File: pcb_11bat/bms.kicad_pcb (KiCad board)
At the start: 2 copper layers, 187 parts, among them CON1 USB-MINI-B, IC1 ATMEGA168PA-M, K1 CONN_3, K2 CONN_3, P1 CONN_1, P10 CONN_1, P11 CONN_1, P12 CONN_1, P13 CONN_1, P14 CONN_1, P15 CONN_1, P16 CONN_1, P17 CONN_1, P18 CONN_1, P19 CONN_1, P2 CONN_1, P20 CONN_1, P21 CONN_2, P22 CONN_1, P23 CONN_1, P3 CONN_1, P4 CONN_1, P5 CONN_1, P6 CONN_1, P7 CONN_3X2, P8 CONN_1, P9 CONN_1, Q1 BC550, Q10 NTD5867, Q11 NTD5867, Q12 NTD5867, Q13 NTD5867, Q14 BC550, Q2 NTD5867, Q3 NTD5867, Q4 NTD5867, Q5 NTD5867, Q6 NTD5867, Q7 NTD5867, Q8 NTD5867, Q9 NTD5867, SW1 SW_PUSH, U1 OPTO, U2 OPTO, U3 AD7280A, U4 AD7280A, U5 LT3010-5, U6 LTC2630, U7 INA197, U8 HRS1K, U9 FT232RQ, X1 CRYSTAL, X2 CRYSTAL 12Mhz

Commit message: placement before routing & corrected a missing resitor on vlow
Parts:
- added R65: 10K, SM0805, F.Cu at (166.5, 68.0)
- added R66: 10K, SM0805, F.Cu at (109.5, 79.0)
- C49: footprint SM0805 -> SMDHD/VF
- moved P2 291.8 mm to (336.5, 88.5)
- moved P3 287.8 mm to (331.0, 88.5)
- moved P21 247.9 mm to (328.0, 51.0)
- moved U2 240.5 mm to (295.0, 51.0), turned to 180 degrees
- moved R42 238.7 mm to (56.5, 81.0)
- moved Q10 236.9 mm to (72.0, 63.0)
- moved U6 233.9 mm to (327.5, 59.0)
- moved U1 231.3 mm to (285.0, 42.0)
- moved P15 229.2 mm to (52.0, 88.0)
- moved K1 226.7 mm to (269.5, 46.0)
- moved P16 219.6 mm to (62.0, 88.0)
- moved P17 209.8 mm to (72.0, 88.5)
- moved SW1 201.8 mm to (277.5, 142.0), turned to 270 degrees
- moved P18 200.4 mm to (82.0, 88.0)
- moved R43 198.7 mm to (66.5, 81.0)
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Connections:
- C21 pad 2: /AD7280A/AD7280A_SUB_LOW/LOBAT -> /AD7280A/AD7280A_SUB_LOW/VIN0
- C35 pad 2: /AD7280A/AD7280A_SUB_LOW/HIBAT -> /AD7280A/AD7280A_SUB_HI/VIN0
- U3 pad 13: /AD7280A/AD7280A_SUB_LOW/LOBAT -> /AD7280A/AD7280A_SUB_LOW/VIN0
- U4 pad 13: /AD7280A/AD7280A_SUB_LOW/HIBAT -> /AD7280A/AD7280A_SUB_HI/VIN0
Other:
- copper layers 2 -> 4
- net class power added: clearance 0.5, trace_width 1, via_dia 0.889, via_drill 0.635
- net class shunts added: clearance 1, trace_width 1.5, via_dia 0.889, via_drill 0.635

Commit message: fixed misplaced caps on the vins, changed some pins assignations on the avr and routed
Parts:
- added R67: 0R, SM0805, F.Cu at (60.5, 135.0)
- added R68: 0R, SM0805, F.Cu at (114.4, 134.6)
- added R69: 0R, SM0805, F.Cu at (52.5, 135.0)
- K1: value CONN_3 -> CHARGER GND 12V SHUT
- K2: value CONN_3 -> REL NC VBAT
- P10: value CONN_1 -> BAT5+
- P11: value CONN_1 -> BAT4+
- P12: value CONN_1 -> BAT3+
- P13: value CONN_1 -> BAT2+
- P14: value CONN_1 -> BAT1+
- P15: value CONN_1 -> VBAT+
- P16: value CONN_1 -> BAT11+/SHUNT
- P17: value CONN_1 -> BAT10+
- P18: value CONN_1 -> BAT9+
- P19: value CONN_1 -> BAT8+
- P20: value CONN_1 -> BAT7+
- P21: value CONN_2 -> GAUGE
- P22: value CONN_1 -> SHUNT
- P23: value CONN_1 -> BAT+
- P8: value CONN_1 -> VBAT GND
- P9: value CONN_1 -> BAT6+
- SP1: value SPEAKER -> BUZZER
- moved D5 159.1 mm to (140.6, 90.6)
- moved C46 152.0 mm to (144.4, 90.4)
- moved R5 145.5 mm to (188.0, 136.7), turned to 180 degrees
- moved U5 145.3 mm to (146.2, 92.0)
- moved C45 138.9 mm to (151.8, 89.5), turned to 270 degrees
- moved P2 138.2 mm to (211.5, 147.5)
- moved R6 135.7 mm to (187.2, 131.1), turned to 270 degrees
- moved C44 135.0 mm to (153.8, 89.5), turned to 270 degrees
- moved U1 133.3 mm to (195.7, 140.9), turned to 180 degrees
- moved C47 133.0 mm to (205.1, 99.3), turned to 180 degrees
- moved U2 132.4 mm to (190.2, 131.9), turned to 0 degrees
- moved R1 126.7 mm to (195.7, 136.4), turned to 90 degrees
- moved U6 126.4 mm to (205.7, 92.8), turned to 180 degrees
- moved P21 125.2 mm to (211.2, 96.0), turned to 270 degrees
- moved C4 121.8 mm to (202.2, 138.9), turned to 270 degrees
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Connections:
- C16 pad 2: N-00000108 (its old number) -> N-00000131
- C17 pad 1: /AD7280A/AD7280A_SUB_LOW/VIN5 -> N-00000131
- C17 pad 2: N-0000097 (its old number) -> /AD7280A/AD7280A_SUB_LOW/VIN4
- C18 pad 2: N-0000094 (its old number) -> /AD7280A/AD7280A_SUB_LOW/VIN3
- C19 pad 2: N-00000103 -> /AD7280A/AD7280A_SUB_LOW/VIN2
- C20 pad 2: N-00000122 (its old number) -> /AD7280A/AD7280A_SUB_LOW/VIN1
- C30 pad 2: N-00000169 -> N-00000168
- C31 pad 1: /AD7280A/AD7280A_SUB_HI/VIN5 -> N-00000168
- C31 pad 2: N-00000170 -> /AD7280A/AD7280A_SUB_HI/VIN4
- C32 pad 2: N-00000173 -> /AD7280A/AD7280A_SUB_HI/VIN3
- C33 pad 2: N-00000171 (its old number) -> /AD7280A/AD7280A_SUB_HI/VIN2
- C34 pad 2: N-00000167 (its old number) -> /AD7280A/AD7280A_SUB_HI/VIN1
- CON1 pad 4: N-0000081 -> (no net)
- CON1 pad 6: /usbserial/SHELL -> /AD7280A/GND
- CON1 pad 7: /usbserial/SHELL -> /AD7280A/GND
- CON1 pad 8: /usbserial/SHELL -> /AD7280A/GND
- CON1 pad 9: /usbserial/SHELL -> /AD7280A/GND
- IC1 pad 1: /CHARGER_ON/ -> /AD7280A/CS/
- IC1 pad 10: /LEDBALANCING -> /LEDERROR
- IC1 pad 11: /LEDERROR -> /BUZZER
- IC1 pad 12: /AD7280A/CS/ -> /STOP_CHARGER
- IC1 pad 13: /BUZZER -> /CHARGER_ON/
- IC1 pad 14: /AD7280A/PD/ -> /comandsolenoid/COILON
- IC1 pad 2: /gauge/CSDAC/ -> /AD7280A/PD/
- IC1 pad 23: /AD7280A/CNVST/ -> (no net)
- IC1 pad 24: (no net) -> /gauge/CSDAC/
- IC1 pad 25: (no net) -> /usbserial/REQUESTTOSEND
- IC1 pad 26: /usbserial/REQUESTTOSEND -> /usbserial/CLEARTOSEND
- IC1 pad 27: /usbserial/CLEARTOSEND -> (no net)
- IC1 pad 28: /comandsolenoid/COILON -> /AD7280A/CNVST/
- IC1 pad 9: /STOP_CHARGER -> /LEDBALANCING
- P10 pad 1: N-00000108 (its old number) -> N-00000106
- P11 pad 1: N-0000097 (its old number) -> N-0000096
- P12 pad 1: N-0000094 (its old number) -> N-00000103
- P13 pad 1: N-00000103 -> N-00000101
- P14 pad 1: N-00000122 (its old number) -> N-00000125
- P18 pad 1: N-00000173 -> N-00000172
- P19 pad 1: N-00000171 (its old number) -> N-00000173
- P20 pad 1: N-00000167 (its old number) -> N-00000166
- Q10 pad 3: N-00000173 -> N-00000172
- Q11 pad 3: N-00000171 (its old number) -> N-00000173
- Q12 pad 3: N-00000167 (its old number) -> N-00000166
- Q2 pad 3: N-00000108 (its old number) -> N-00000106
- Q3 pad 3: N-0000097 (its old number) -> N-0000096
- Q4 pad 3: N-0000094 (its old number) -> N-00000103
- Q5 pad 3: N-00000103 -> N-00000101
- Q6 pad 3: N-00000122 (its old number) -> N-00000125
- R24 pad 1: N-00000108 (its old number) -> N-00000106
- R25 pad 1: N-0000097 (its old number) -> N-0000096
- R26 pad 1: N-0000094 (its old number) -> N-00000103
- R27 pad 1: N-00000103 -> N-00000101
- R28 pad 1: N-00000122 (its old number) -> N-00000125
- R30 pad 1: N-00000108 (its old number) -> N-00000106
- R30 pad 2: /AD7280A/AD7280A_SUB_LOW/VIN5 -> N-00000131
- R31 pad 1: N-0000097 (its old number) -> N-0000096
- R32 pad 1: N-0000094 (its old number) -> N-00000103
- R33 pad 1: N-00000103 -> N-00000101
- R34 pad 1: N-00000122 (its old number) -> N-00000125
- R45 pad 1: N-00000173 -> N-00000172
- R46 pad 1: N-00000171 (its old number) -> N-00000173
- R47 pad 1: N-00000167 (its old number) -> N-00000166
- R49 pad 2: /AD7280A/AD7280A_SUB_HI/VIN5 -> N-00000168
- R51 pad 1: N-00000173 -> N-00000172
- R52 pad 1: N-00000171 (its old number) -> N-00000173
- R53 pad 1: N-00000167 (its old number) -> N-00000166
- R61 pad 1: N-0000081 -> /AD7280A/AD7280A_SUB_LOW/VIN4
- R61 pad 2: /AD7280A/GND -> /AD7280A/AD7280A_SUB_LOW/VIN5
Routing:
- net /AD7280A/GND: track 0.00 -> 424.1 mm, vias 0 -> 13
- net /SHIELD: track 0.00 -> 322.0 mm
- net /CSense/5V: track 0.00 -> 233.4 mm, vias 0 -> 8
- net /AD7280A/AD7280A_SUB_LOW/VDDNFILTERED: track 0.00 -> 230.7 mm, vias 0 -> 4
- net /AD7280A/VBAT: track 0.00 -> 186.5 mm, vias 0 -> 4
- net /AD7280A/AD7280A_SUB_LOW/HIBAT: track 0.00 -> 126.8 mm, vias 0 -> 1
- net /AD7280A/SCLK: track 0.00 -> 126.7 mm, vias 0 -> 4
- net /AD7280A/SDI: track 0.00 -> 123.4 mm, vias 0 -> 4
- net /AD7280A/AD7280A_SUB_LOW/VIN2: track 0.00 -> 100.2 mm, vias 0 -> 3
- net /AD7280A/AD7280A_SUB_LOW/VIN1: track 0.00 -> 93.0 mm, vias 0 -> 3
- net /AD7280A/AD7280A_SUB_LOW/LOBAT: track 0.00 -> 89.9 mm, vias 0 -> 2
- net /AD7280A/SDO: track 0.00 -> 83.3 mm, vias 0 -> 2
- net /AD7280A/AD7280A_SUB_LOW/VIN3: track 0.00 -> 83.0 mm, vias 0 -> 3
- net /AD7280A/AD7280A_SUB_LOW/VIN0: track 0.00 -> 77.8 mm, vias 0 -> 2
- net /AD7280A/AD7280A_SUB_HI/VIN6: track 0.00 -> 75.2 mm, vias 0 -> 2
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- added copper zone on B.Cu, net /AD7280A/AD7280A_SUB_LOW/VDDNFILTERED
- added copper zone on F.Cu, net /AD7280A/AD7280A_SUB_LOW/VDDNFILTERED
- added copper zone on B.Cu, net /AD7280A/GND
- added copper zone on F.Cu, net /AD7280A/GND
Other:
- board outline added: 179.5 x 67 mm
- copper layers 4 -> 2
- net class Default: clearance 0.254 -> 0.1
- net class Oldefault added: clearance 0.254, trace_width 0.254, via_dia 0.889, via_drill 0.635
- net class halfpower added: clearance 0.254, trace_width 0.354, via_dia 0.889, via_drill 0.635
- net class micro added: clearance 0.125, trace_width 0.254, via_dia 0.889, via_drill 0.635
- rule trace_clearance: 0.254 -> 0.1

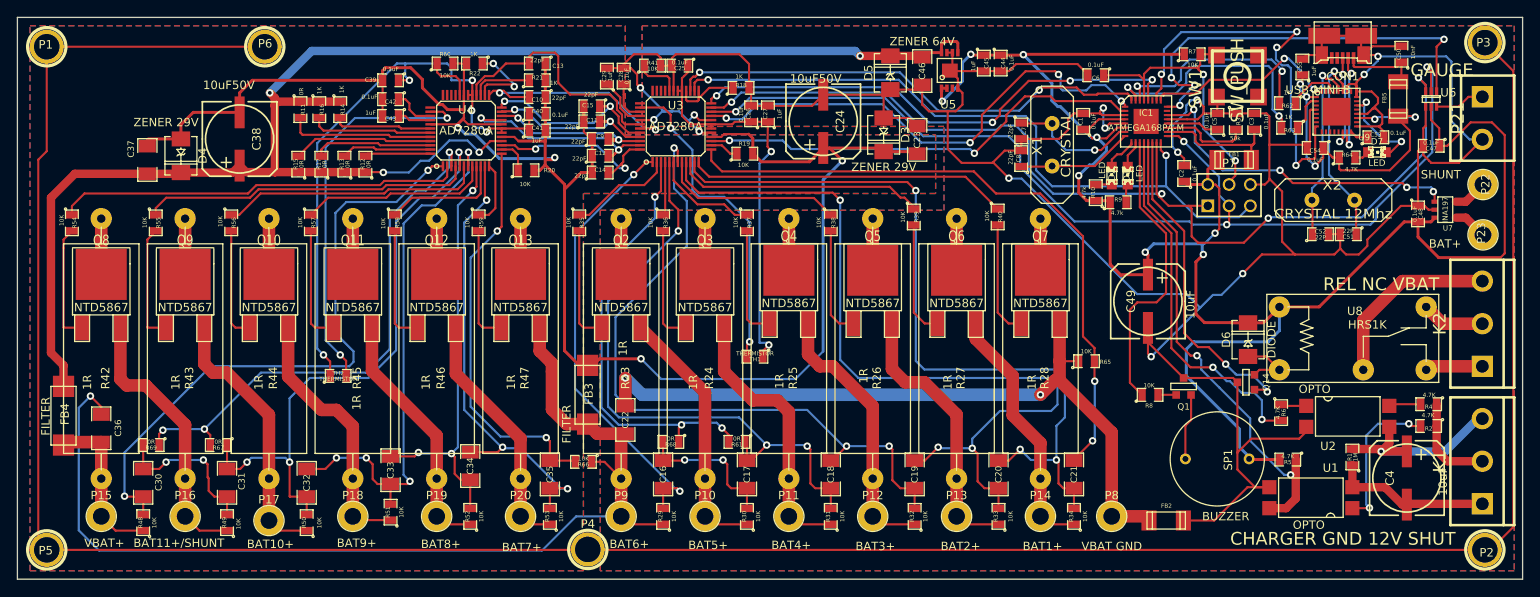
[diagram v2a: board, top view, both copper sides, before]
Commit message: sent to production, buzeer pad drill change, changed vias diameter
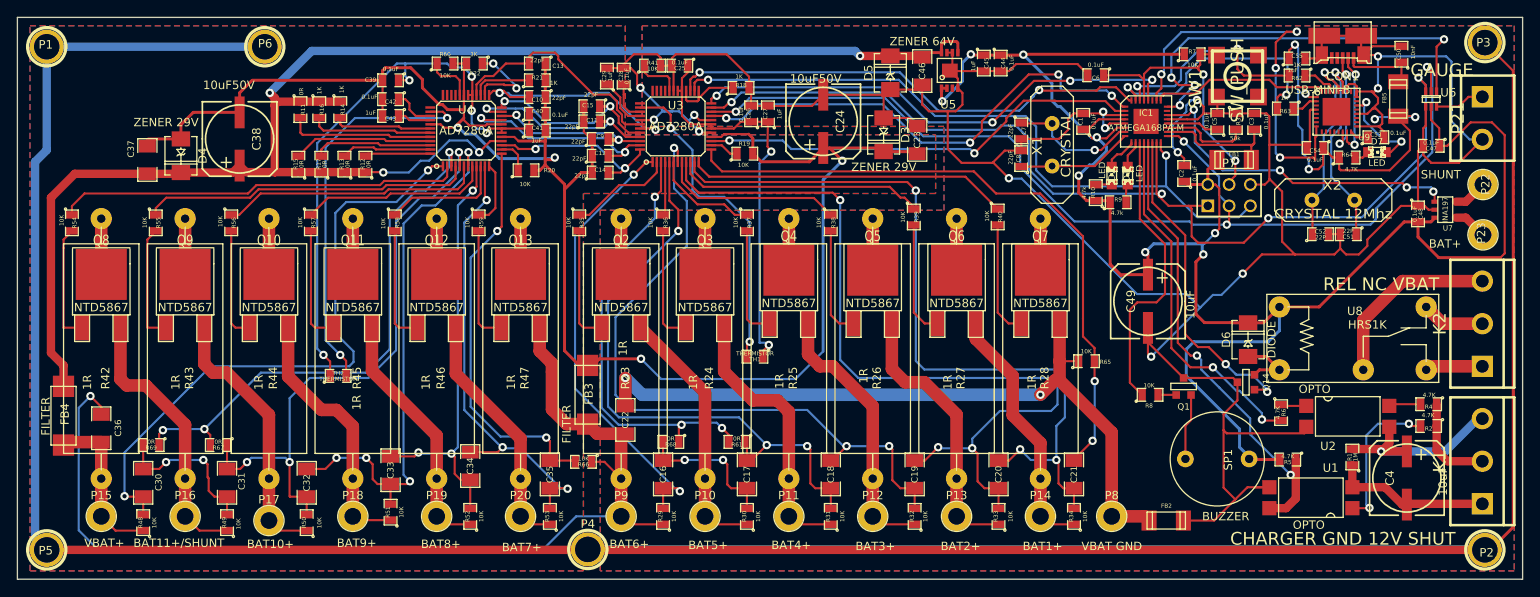
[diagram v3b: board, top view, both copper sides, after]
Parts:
- moved R62 3.49 mm to (189.1, 90.9)
- moved R63 2.34 mm to (187.7, 94.9)
- moved C55 1.20 mm to (189.1, 88.9), turned to 0 degrees
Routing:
- net /SHIELD: track 322.0 -> 429.3 mm
- net /usbserial/USBVCC: track 42.5 -> 48.9 mm
- net /AD7280A/AD7280A_SUB_HI/SDI: track 21.1 -> 24.8 mm
- net /usbserial/REQUESTTOSEND: track 23.5 -> 21.1 mm, vias 2 -> 0
- net N-0000088: track 6.27 -> 4.24 mm
- net N-0000086: track 22.6 -> 24.4 mm
- net /AD7280A/AD7280A_SUB_HI/ALERT_IO: track 29.3 -> 27.7 mm
- net /AD7280A/CS/: track 60.0 -> 58.6 mm
- net N-0000087: track 4.47 -> 3.10 mm
- net /usbserial/TXD: track 29.1 -> 30.4 mm
- net /AD7280A/AD7280A_SUB_HI/SDO: track 9.79 -> 10.8 mm
- net /STOP_CHARGER: track 43.9 -> 43.0 mm
- net /AD7280A/AD7280A_SUB_HI/PD/: track 22.2 -> 21.5 mm
- net N-0000082: track 12.3 -> 13.0 mm
- net /AD7280A/PD/: track 54.0 -> 53.3 mm
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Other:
- net class Default: via_dia 0.889 -> 1
- net class Oldefault: via_dia 0.889 -> 1
- net class halfpower: via_dia 0.889 -> 1
- net class micro: via_dia 0.889 -> 1
- net class power: via_dia 0.889 -> 1
- net class shunts: via_dia 0.889 -> 1

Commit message: Soldering components on the prototype, some changes on the schematics and component values
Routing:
- net /usbserial/USBVCC: track 48.9 -> 51.1 mm
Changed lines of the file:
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@@
   (general
     (links 382)
-    (no_connects 1)
+    (no_connects 0)
     (area 35.486334 83.066735 216.163401 151.929)
     (thickness 1.6)
     (drawings 4)
-    (tracks 1892)
+    (tracks 1894)
     (zones 0)
     (modules 192)
@@
   (segment (start 187.071 93.218) (end 187.833 93.218) (width 0.254) (layer F.Cu) (net 88))
   (segment (start 186.7535 93.5355) (end 187.071 93.218) (width 0.254) (layer F.Cu) (net 88))
+  (segment (start 196.2023 95.9993) (end 198.2343 95.9993) (width 0.254) (layer F.Cu) (net 89) (status 400000))
+  (segment (start 198.2343 95.9993) (end 198.374 96.139) (width 0.254) (layer F.Cu) (net 89))
   (segment (start 188.1505 88.9) (end 188.1505 87.9475) (width 0.254) (layer F.Cu) (net 89))
   (segment (start 189.23 87.63) (end 189.23 92.964) (width 0.254) (layer B.Cu) (net 89))
